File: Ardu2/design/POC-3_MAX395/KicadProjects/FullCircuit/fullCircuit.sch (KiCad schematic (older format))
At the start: 128 parts, among them P1 CONN_01X02, P2 CONN_01X14, P3 CONN_01X14, P4 CONN_01X01, P7 CONN_01X15, U1 Pyboard, U10 MAX395, U11 MAX395, U12 MAX395, U13 MAX395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

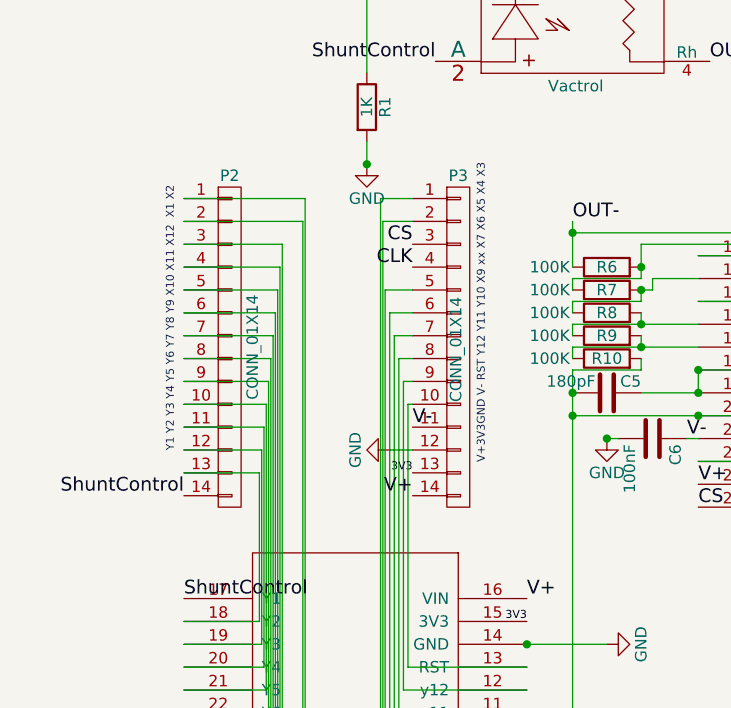
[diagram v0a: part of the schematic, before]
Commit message: created a new peripherals PCB
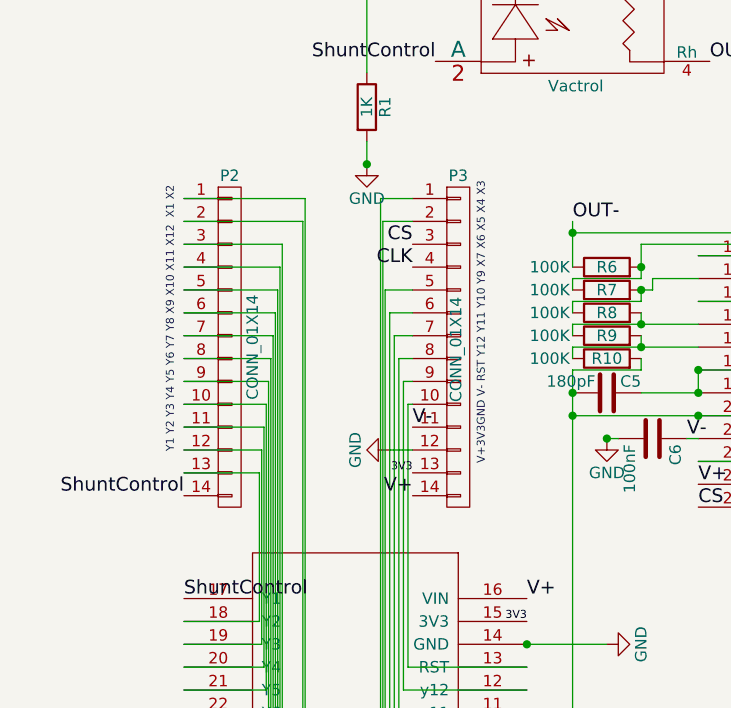
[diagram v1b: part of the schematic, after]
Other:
- note added: "V+3V3GND V- RST Y12 Y11 Y10 Y9 X7 X6 X5 X4 X3"
- note added: "Y1 Y2 Y3 Y4 Y5 Y6 Y7 Y8 X9 X10 X11 X12 X1 X2"
- note removed: "V+3V3GND V- RST Y12 Y11 Y10 X9 xx X7 X6 X5 X4 X3"
- note removed: "Y1 Y2 Y3 Y4 Y5 Y6 Y7 Y8 Y9 X10 X11 X12 X1 X2"
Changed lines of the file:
@@
 Sheet 1 1
 Title "ArduGuitar Full Circuit MAX395"
-Date "2015-11-04"
-Rev "1.8"
+Date "2016-10-22"
+Rev "1.8.1"
 Comp "www.arduguitar.org"
-Comment1 "update after review,"
-Comment2 "added V+/V- to headers"
-Comment3 "changed VGA Connector footprint"
-Comment4 "addec schottkey to prevent LM2596 latch-up"
+Comment1 "added V+/V- to headers"
+Comment2 "changed VGA Connector footprint"
+Comment3 "addec schottkey to prevent LM2596 latch-up"
+Comment4 "changed pinout on header Y9->X9"
 $EndDescr
 $Comp
@@
 ShuntControl
 Text Notes 710  1800 3    35   ~ 0
-Y1 Y2 Y3 Y4 Y5 Y6 Y7 Y8 Y9 X10 X11 X12  X1 X2
-Text Notes 2070 1700 3    35   ~ 0
-V+3V3GND V- RST Y12 Y11 Y10 X9 xx X7 X6 X5 X4 X3
+Y1 Y2 Y3 Y4 Y5 Y6 Y7 Y8 X9 X10 X11 X12  X1 X2
+Text Notes 2070 1780 3    35   ~ 0
+V+3V3GND V- RST Y12 Y11 Y10 Y9 X7 X6 X5 X4 X3
 Text Label 6150 7500 2    35   ~ 0
 DoutSpare
